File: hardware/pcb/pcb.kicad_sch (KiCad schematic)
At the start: 39 parts, among them Q1 FQD50N06, Q2 FQD50N06

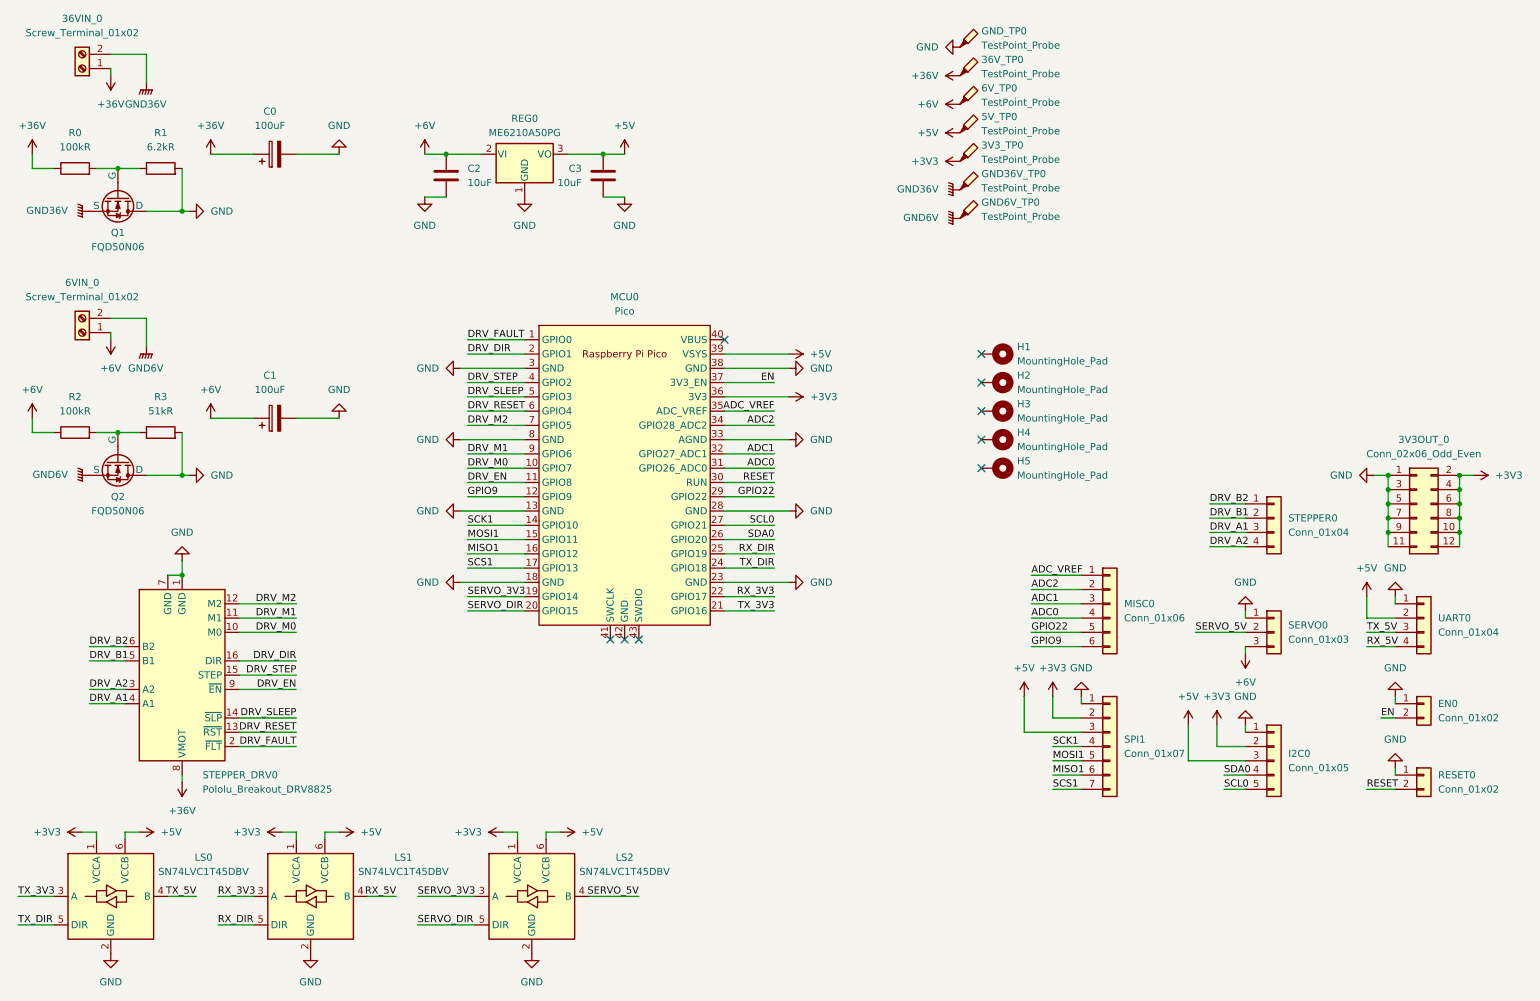
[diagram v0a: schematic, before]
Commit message: fixed my stupid mistake, reverse polarity protection should work now
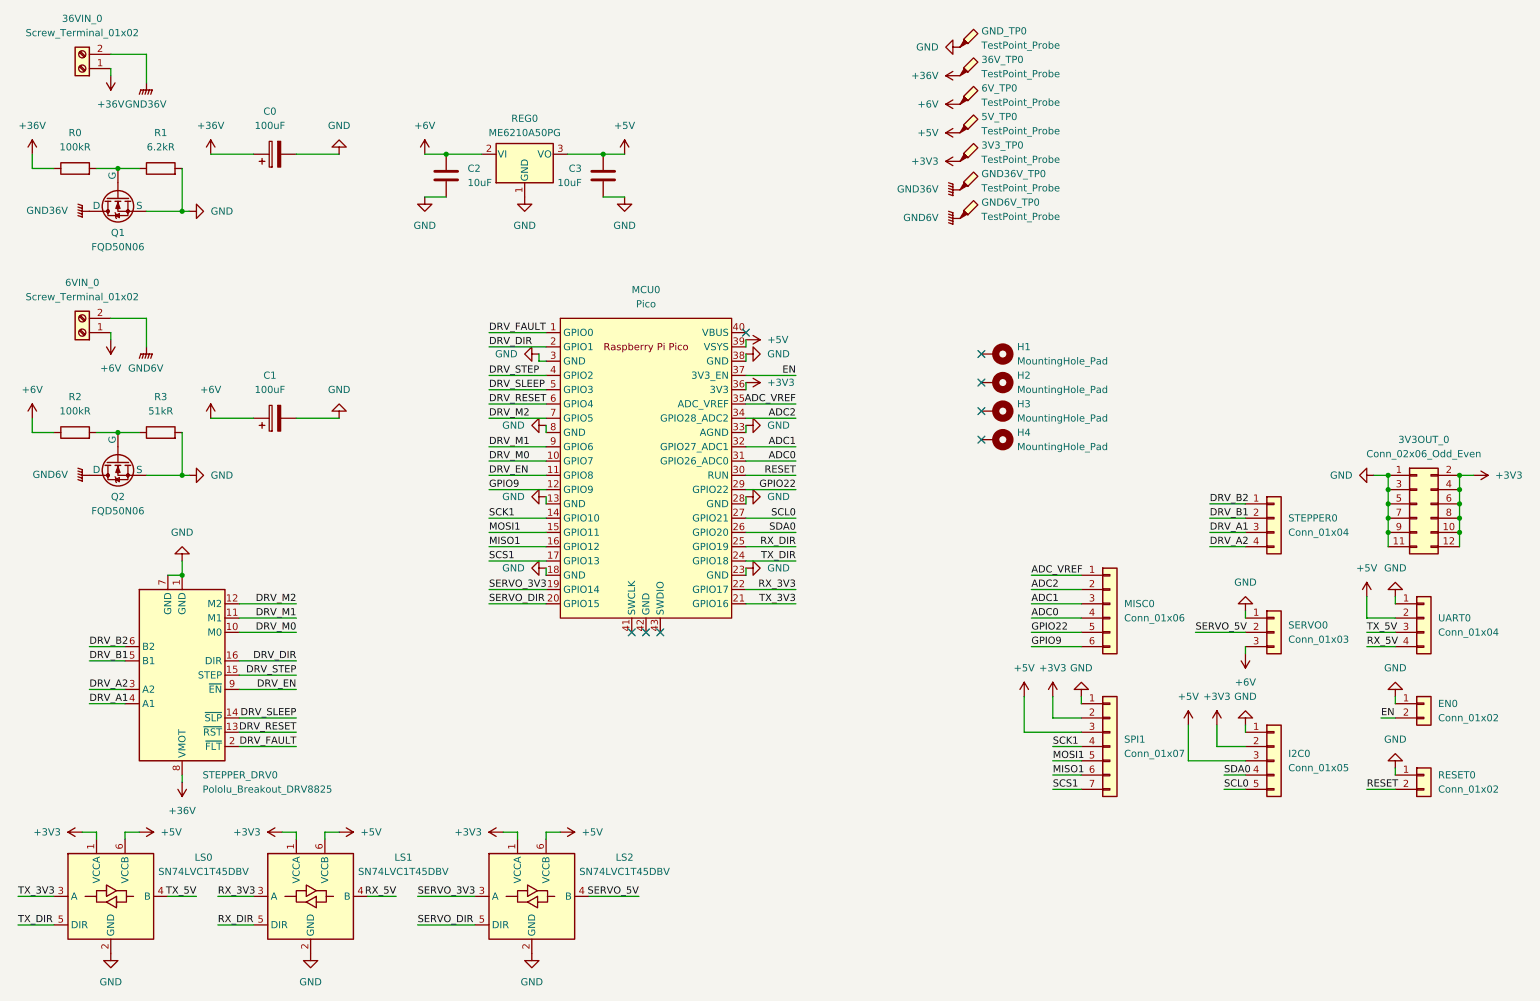
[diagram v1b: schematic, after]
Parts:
- removed H5: MountingHole_Pad, MountingHole:MountingHole_3.2mm_M3_Pad_Via, symbol Mechanical:MountingHole_Pad
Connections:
- net GND: now also Q1.3 (S), Q2.3 (S); no longer Q1.1 (D), Q2.1 (D)
- net GND36V: now also Q1.1 (D); no longer Q1.3 (S)
- net GND6V: now also Q2.1 (D); no longer Q2.3 (S)
- no-connect marks 9 -> 8
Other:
- moved on the sheet: MCU0, Q1, Q2
